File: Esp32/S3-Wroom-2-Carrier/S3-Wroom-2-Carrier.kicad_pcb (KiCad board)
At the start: 2 copper layers, 35.8 x 39.4 mm, 17 parts, among them J2 65100516121, J4 DF9B-21S-1V69, J5 DF9B-21S-1V69, U2 ADM7171ACPZ-3.0-R7

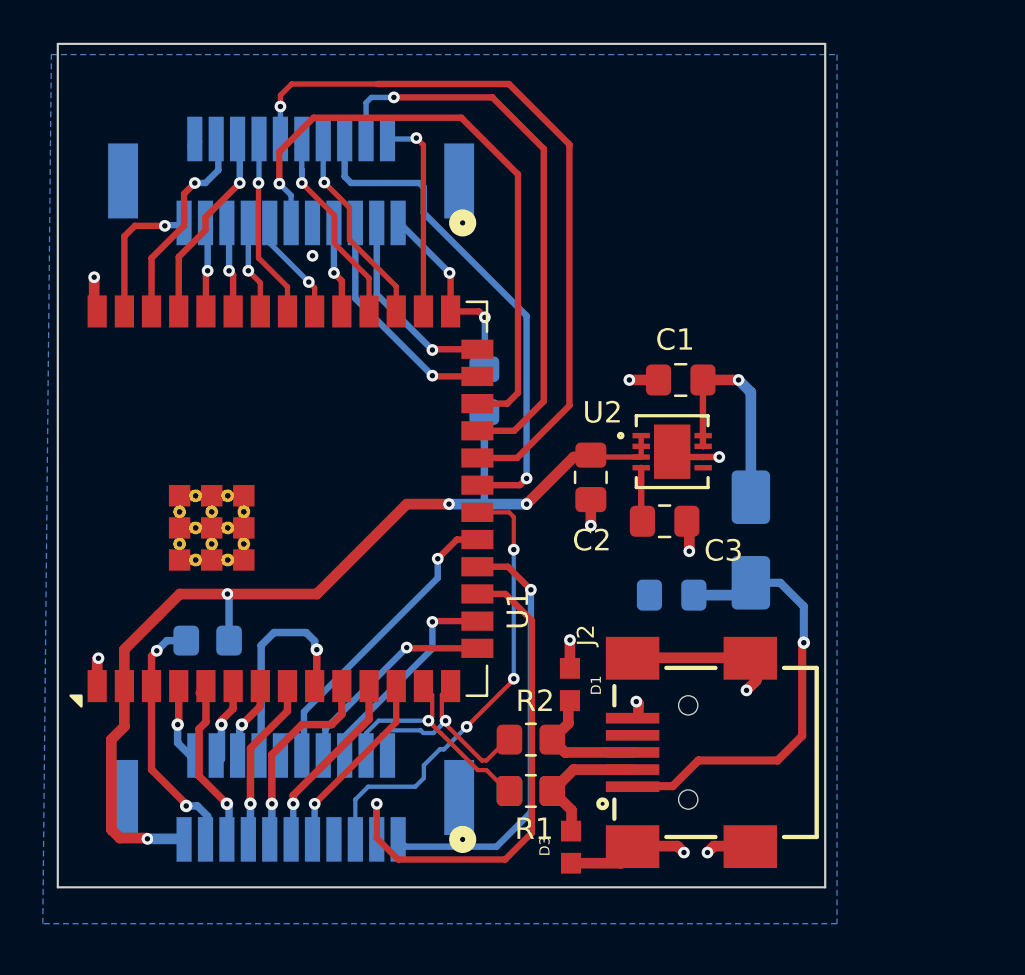
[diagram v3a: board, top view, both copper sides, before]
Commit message: two layer board
Final 2 layer board
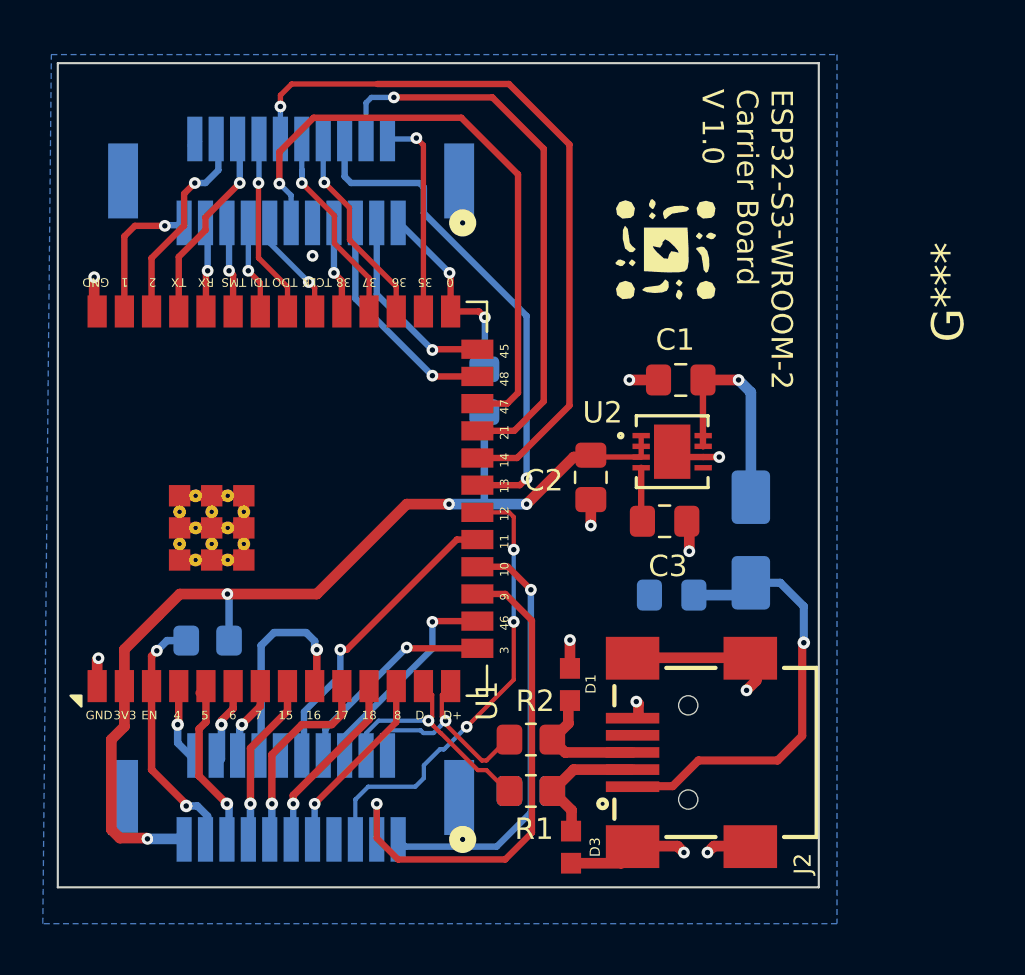
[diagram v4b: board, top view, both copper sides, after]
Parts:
- added G***: LOGO, LOGO, F.Cu at (163.9, 88.1)
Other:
- board size 35.8 x 39.4 mm -> 35.6 x 38.5 mm
- board text added: "0"
- board text added: "1"
- board text added: "10"
- board text added: "11"
- board text added: "12"
- board text added: "13"
- board text added: "14"
- board text added: "15"
- board text added: "16"
- board text added: "17"
- board text added: "18"
- board text added: "2"
- board text added: "21"
- board text added: "3"
- board text added: "35"
- board text added: "36"
- board text added: "37"
- board text added: "38"
- board text added: "3V3"
- board text added: "4"
- board text added: "45"
- board text added: "46"
- board text added: "47"
- board text added: "48"
- board text added: "5"
- board text added: "6"
- board text added: "7"
- board text added: "8"
- board text added: "9"
- board text added: "D+"
- board text added: "D-"
- board text added: "EN"
- board text added: "ESP32-S3-WROOM-2 Carrier Board V 1.0"
- board text added: "GND"
- board text added: "RX"
- board text added: "TCLK"
- board text added: "TDI"
- board text added: "TDO"
- board text added: "TMS"
- board text added: "TX"

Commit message: Connectors
change one connector from 21 to 25 pins
Added test points
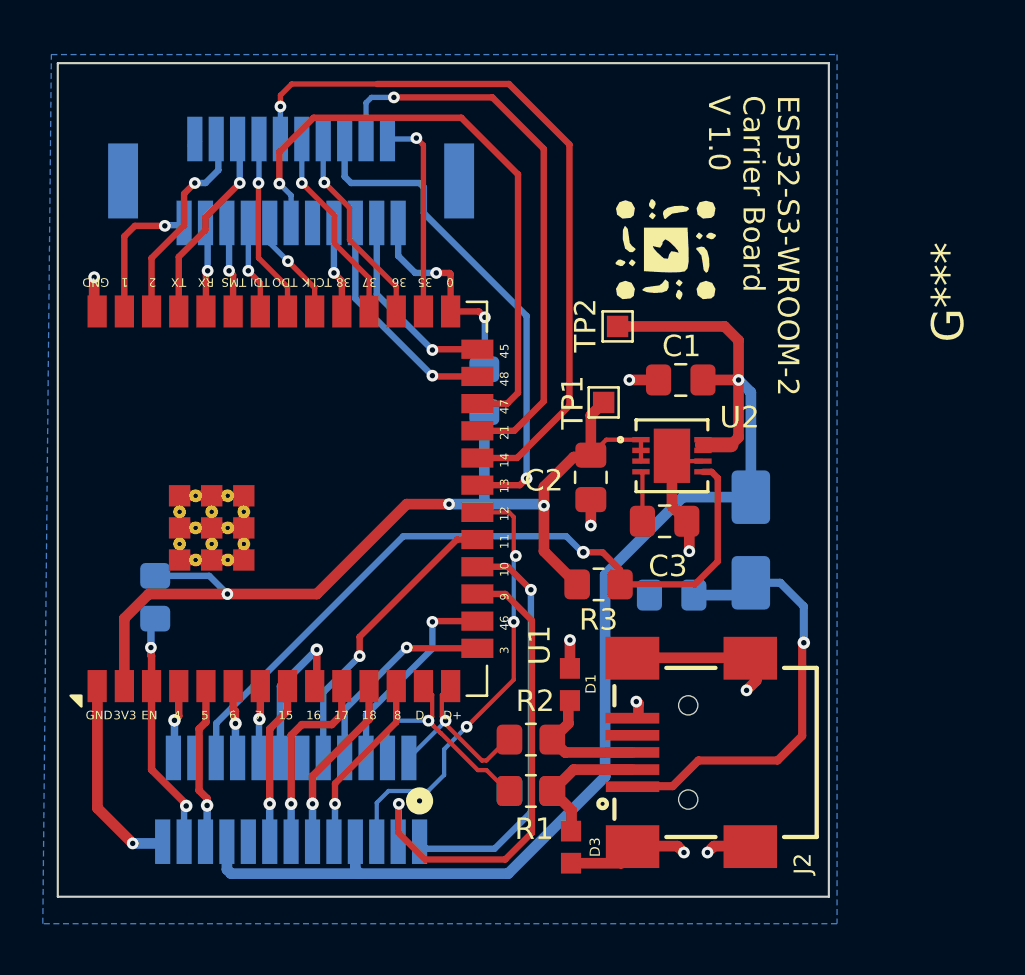
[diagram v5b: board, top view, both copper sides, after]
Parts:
- removed J4: DF9B-21S-1V69, User_Footprint:CONN_DF9B-21S-1V_21P_HIR
- added J1: DF9B-25S-1V32, User_Footprint:CON9_1X25_DL_DF9_HIR, B.Cu at (146.4, 113.8)
- added R3: 100K, Resistor_SMD:R_0805_2012Metric_Pad1.20x1.40mm_HandSolder, F.Cu at (160.8, 103.8)
- added TP1: 3V3, TestPoint:TestPoint_Pad_1.0x1.0mm, F.Cu at (161.0, 95.2)
- added TP2: VIN, TestPoint:TestPoint_Pad_1.0x1.0mm, F.Cu at (161.7, 91.7)
- moved R5 3.18 mm to (140.1, 104.3), turned to -90 degrees
- moved U2 0.19 mm to (164.2, 97.7)
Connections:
- net /Project Architecture/Power/VIN renamed /Project Architecture/VIN
- U2 pad 5: /Project Architecture/Power/EN -> /Project Architecture/PWR_EN
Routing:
- net /Project Architecture/VIN: track 11.0 -> 59.9 mm
- net /Project Architecture/PWR_EN: track 0.00 -> 35.2 mm, vias 0 -> 1
- net GND: track 38.3 -> 49.0 mm, vias 12 -> 10
- net /Project Architecture/Break Out Connection/GPIO16: track 10.6 -> 7.50 mm
- net /Project Architecture/Break Out Connection/USB_D+: track 10.8 -> 8.56 mm
- net /Project Architecture/Break Out Connection/GPIO8: track 9.05 -> 7.80 mm
- net /Project Architecture/Break Out Connection/GPIO5: track 8.63 -> 7.59 mm
- net /Project Architecture/Break Out Connection/GPIO9: track 24.4 -> 23.4 mm
- net /Project Architecture/Break Out Connection/GPIO10: track 20.3 -> 19.4 mm
- net /Project Architecture/EN: track 12.2 -> 11.3 mm
- net /Project Architecture/Break Out Connection/GPIO0: track 9.34 -> 10.2 mm
- net /Project Architecture/Break Out Connection/GPIO46: track 11.2 -> 10.4 mm
- net /Project Architecture/Break Out Connection/GPIO11: track 14.5 -> 13.7 mm
- net /Project Architecture/Break Out Connection/GPIO37: track 9.97 -> 9.36 mm
- net /Project Architecture/Break Out Connection/GPIO3: track 10.2 -> 10.8 mm
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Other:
- board size 35.6 x 38.5 mm -> 36 x 38.9 mm
